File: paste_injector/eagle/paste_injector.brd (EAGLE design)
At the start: 40 x 30 mm, 20 parts, among them IC1 ULN2003AD, J2 USB, J5 PINHD-2X3, Q2 CSTCR6M00G53Z, U2 FT232RL, U4 ATMEGA328TQFP32

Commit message: Work in progress.
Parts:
- removed C5, C6, C7: 0.1uF, paste_injector:C0603
- removed U$28: OSH, paste_injector:OSH
- removed U2: FT232RL, paste_injector:SSOP28DB
- added C1: 0.1uF, paste_injector:C0603
- added JP2: (no value), paste_injector:1X06
- R10, R2: value 10K -> 5K
- moved R10 14.9 mm to (22.1, 5.74), turned to 270 degrees
- moved C3 14.3 mm to (6.01, 9.26), turned to 180 degrees
- moved U4 7.93 mm to (15.8, 14.1)
- moved C10 6.93 mm to (23.7, 12.6), turned to 90 degrees
- moved Q2 6.19 mm to (14.1, 22.0)
- moved C2 5.72 mm to (7.68, 16.3), turned to 270 degrees
- moved JP1 5.12 mm to (27.7, 27.9)
- moved IC1 4.92 mm to (28.9, 19.4), turned to 0 degrees
- moved LED1 1.38 mm to (16.4, 27.2)
- moved J5 0.90 mm to (4.45, 26.7)
- moved R1 0.64 mm to (31.8, 5.08)
- moved R2 0.45 mm to (12.4, 27.3)
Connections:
- removed net N$11: C6.1, U2.2
- removed net N$16: C7.1, U2.17
- removed net SER_RX: U2.1, U4.30
- removed net SER_TX: U2.5, U4.31
- removed net USB_DM: J2.2, U2.16
- removed net USB_DP: J2.3, U2.15
- new net DTR: C1.2, JP2.6
- new net RXI: JP2.4, U4.30
- new net TXO: JP2.5, U4.31
- net +5V: now also JP2.3; no longer C5.1, U2.20, U2.4
- net GND: now also JP2.1, JP2.2; no longer C5.2, C7.2, U2.18, U2.21, U2.25, U2.26, U2.7
- net RESET: now also C1.1; no longer C6.2

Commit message: Minor tweaks.
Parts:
- removed C10: 0.1uF, paste_injector:C0603
- removed IC1: ULN2003AD, paste_injector:SO16
- removed J5: PINHD-2X3, paste_injector:2X03
- removed JP1: (no value), paste_injector:1X05
- removed JP2: (no value), paste_injector:1X06
- removed LED1: (no value), arm-pro-mini-tester:LED0603
- removed Q2: CSTCR6M00G53Z, paste_injector:CSTCR6M
- removed R10: 5K, paste_injector:R0603
- removed U4: ATMEGA328TQFP32, paste_injector:TQFP32-08
- added C4: 0.1uF, paste_injector:C0603
- added D1: (no value), paste_injector:LED0603
- added ISP: PINHD-2X3, paste_injector:2X03
- added J1: USB, paste_injector:USB-MICRO-ZX62RD-AB-5P8
- added J3: (no value), paste_injector:1X05
- added Q1: CSTCR6M00G53Z, paste_injector:CSTCR6M
- added R3: 5K, paste_injector:R0603
- added U1: ATMEGA328TQFP32, paste_injector:TQFP32-08
- added U2: ULN2003AD, paste_injector:SO16
- C1: value 0.1uF -> 10uF; device paste_injector:C0603 -> paste_injector:A/3216-18R
- C3: value 10uF -> 0.1uF; device paste_injector:A/3216-18R -> paste_injector:C0603
- J2: value USB -> (none); device paste_injector:USB-MICRO-ZX62RD-AB-5P8 -> paste_injector:1X06
- R1: value (none) -> 10K; device paste_injector:CA9V -> paste_injector:TRIMPOT
- S1, S2: device paste_injector:TLE1105 -> paste_injector:PUSH_BUTTON
- moved J2 38.9 mm to (38.0, 21.1)
- moved C3 26.6 mm to (32.4, 12.6), turned to 0 degrees
- moved C1 24.6 mm to (7.94, 15.7), turned to 270 degrees
- moved C2 18.7 mm to (25.8, 11.6)
- moved S2 14.0 mm to (19.7, 4.19)
- moved S1 9.53 mm to (5.71, 4.19)
- moved R1 3.17 mm to (34.9, 5.08), turned to 0 degrees
- moved R2 1.77 mm to (11.7, 25.6)
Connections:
- net +5V: now also C1.+, C4.1, ISP.2, J1.1, J2.3, J3.3, R1.CW, R3.2, U1.18, U1.4, U1.6, U2.9; no longer C10.1, C3.+, IC1.9, J2.1, J5.2, JP1.3, JP2.3, R1.E, R10.2, U4.18, U4.4, U4.6
- net BACKWARD: now also S2.B1, U1.11; no longer S1.B, U4.11
- net DTR: now also C3.2, J2.6; no longer C1.2, JP2.6
- net FORWARD: now also S1.B1, U1.10; no longer S2.B, U4.10
- net GND: now also C1.-, C4.2, D1.C, ISP.6, J1.5, J2.1, J2.2, Q1.2, R1.CCW, S1.A1, S1.GND, S2.A1, S2.GND, U1.21, U1.3, U1.5, U2.5, U2.6, U2.7, U2.8; no longer C10.2, C3.-, IC1.5, IC1.6, IC1.7, IC1.8, J2.5, J5.6, JP2.1, JP2.2, LED1.C, Q2.2, R1.A, S1.A, S2.A, U4.21, U4.3, U4.5
- net M1: now also U1.32, U2.1; no longer IC1.1, U4.25
- net M1-BLUE: now also J3.5, U2.16; no longer IC1.16, JP1.5
- net M2: now also U1.1, U2.2; no longer IC1.2, U4.26
- net M2-PINK: now also J3.4, U2.15; no longer IC1.15, JP1.4
- net M3: now also U1.2, U2.3; no longer IC1.3, U4.19
- net M3-YELOW: now also J3.1, U2.14; no longer IC1.14, JP1.1
- net M4: now also U1.9, U2.4; no longer IC1.4, U4.22
- net M4-ORANGE: now also J3.2, U2.13; no longer IC1.13, JP1.2
- net MISO: now also ISP.1, U1.16; no longer J5.1, U4.16
- net MOSI: now also ISP.4, U1.15; no longer J5.4, U4.15
- net N$1: now also D1.A; no longer LED1.A
- net N$2: now also Q1.1, U1.7; no longer Q2.1, U4.7
- net N$7: now also Q1.3, U1.8; no longer Q2.3, U4.8
- net POT: now also R1.C, U1.23; no longer R1.S, U4.23
- net RESET: now also C3.1, ISP.5, R3.1, U1.29; no longer C1.1, J5.5, R10.1, U4.29
- net RXI: now also J2.4, U1.30; no longer JP2.4, U4.30
- net SCK/LED: now also ISP.3, U1.17; no longer J5.3, U4.17
- net TXO: now also J2.5, U1.31; no longer JP2.5, U4.31
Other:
- outline, holes or cut-outs redrawn
- board text added: "B"
- board text added: "O"
- board text added: "P"
- board text added: "PULL"
- board text added: "PUSH"
- board text added: "R"
- board text added: "REV 0"
- board text added: "SPD"
- board text added: "Y"

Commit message: Performed final routing.
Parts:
- moved S2 2.54 mm to (17.1, 4.19)
- moved C3 1.52 mm to (30.9, 12.6)
- moved R2 1.38 mm to (10.9, 24.5)
- moved Q1 1.36 mm to (15.7, 25.7)
- moved R3 1.19 mm to (22.2, 10.3)
- moved D1 0.84 mm to (7.92, 21.0), turned to 180 degrees
- moved C2 0.48 mm to (25.8, 11.1)
- turned ISP to 0 degrees
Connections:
- net GND: now also J1.A, J1.B, J1.C, J1.D
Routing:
- net +5V: track 0.00 -> 98.2 mm
- net M4: track 0.00 -> 56.8 mm, vias 0 -> 8
- net RESET: track 0.00 -> 46.3 mm, vias 0 -> 4
- net GND: track 0.00 -> 34.6 mm, vias 0 -> 3
- net RXI: track 0.00 -> 34.0 mm, vias 0 -> 2
- net MOSI: track 0.00 -> 28.2 mm, vias 0 -> 2
- net POT: track 0.00 -> 26.8 mm, vias 0 -> 2
- net MISO: track 0.00 -> 20.3 mm, vias 0 -> 4
- net SCK/LED: track 0.00 -> 19.9 mm
- net TXO: track 0.00 -> 19.2 mm, vias 0 -> 3
- net FORWARD: track 0.00 -> 18.7 mm, vias 0 -> 2
- net M2-PINK: track 0.00 -> 17.3 mm, vias 0 -> 2
- net M3: track 0.00 -> 16.4 mm, vias 0 -> 2
- net BACKWARD: track 0.00 -> 16.4 mm, vias 0 -> 2
- net M1-BLUE: track 0.00 -> 15.2 mm
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- added copper zone on layer 16, net GND
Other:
- board text added: "PUSH SPEED"
- board text removed: "SPD"

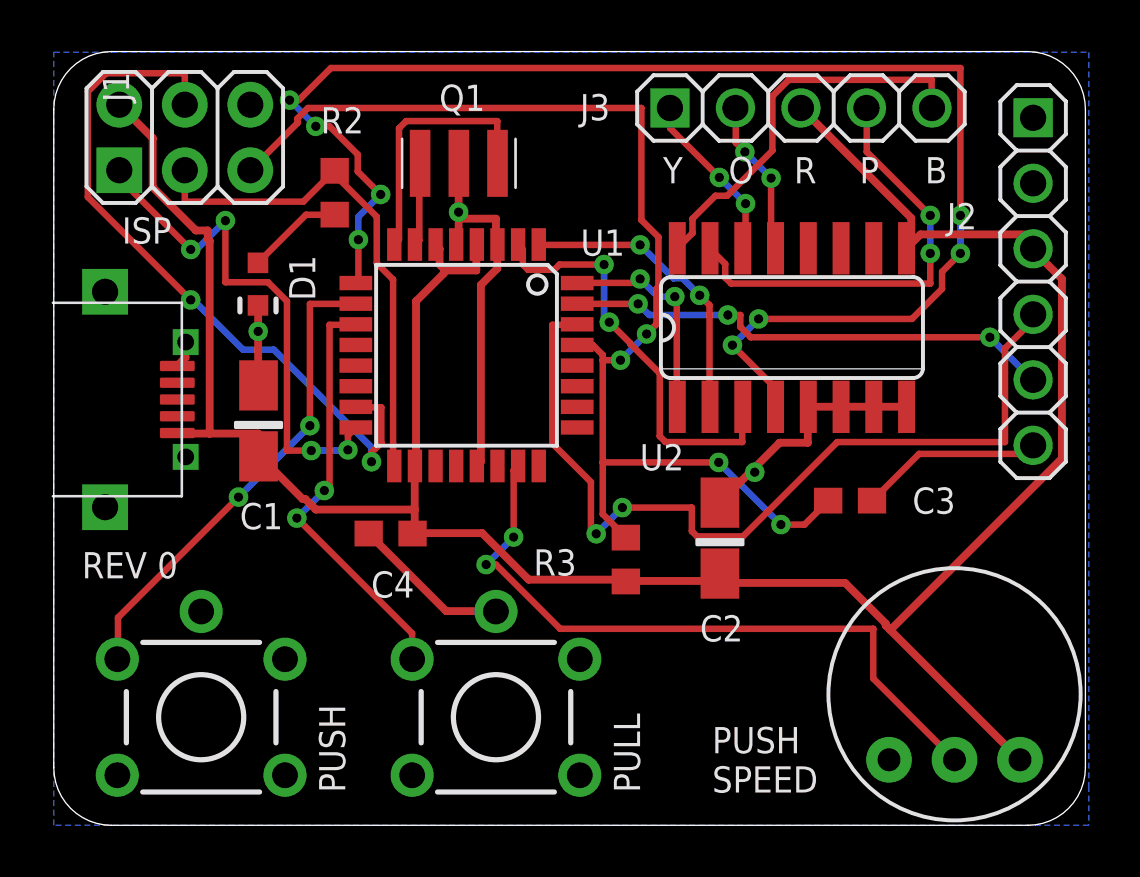
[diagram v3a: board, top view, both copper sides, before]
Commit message: Updated reasonator's footprint.
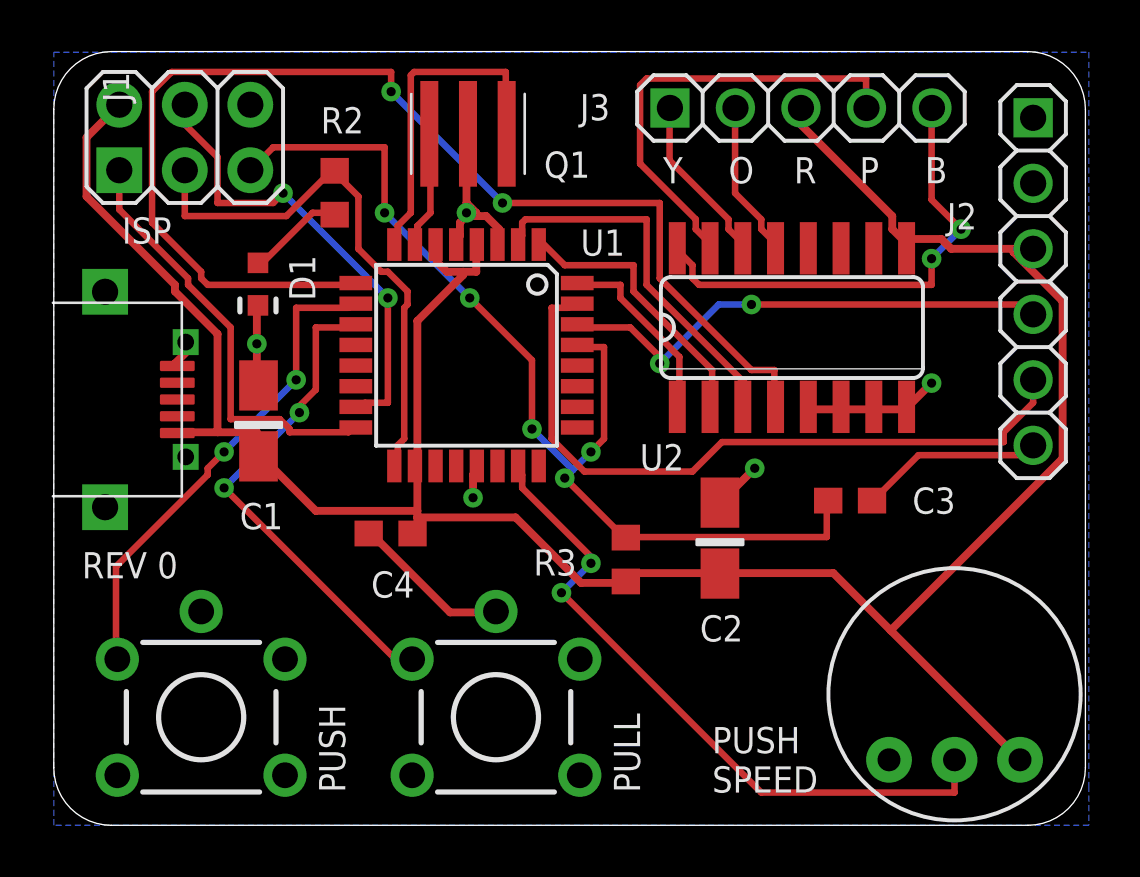
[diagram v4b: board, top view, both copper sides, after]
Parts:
- moved Q1 1.20 mm to (16.1, 26.8)
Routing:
- net RXI: track 34.0 -> 19.8 mm
- net MOSI: track 28.2 -> 18.2 mm
- net M4: track 56.8 -> 47.1 mm, vias 8 -> 2
- net TXO: track 19.2 -> 27.6 mm, vias 3 -> 0
- net GND: track 34.6 -> 26.4 mm, vias 3 -> 5
- net RESET: track 46.3 -> 40.6 mm, vias 4 -> 5
- net MISO: track 20.3 -> 16.7 mm, vias 4 -> 0
- net M1-BLUE: track 15.2 -> 18.7 mm, vias 0 -> 2
- net BACKWARD: track 16.4 -> 19.4 mm
- net N$7: track 10.1 -> 13.1 mm
- net +5V: track 98.2 -> 99.8 mm
- net M3: track 16.4 -> 14.8 mm, vias 2 -> 0
- net SCK/LED: track 19.9 -> 21.4 mm
- net N$2: track 3.23 -> 4.60 mm
- net M1: track 8.54 -> 7.50 mm, vias 2 -> 0
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
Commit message: Added BOM and TODO. Also, minor tweaks.
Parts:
- R2: value 5K -> 3K3
- R3: value 5K -> 10K
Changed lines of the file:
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@@
 <attribute name="NAME" x="2.6444" y="22.5552" size="1.016" layer="25" font="vector" ratio="10"/>
 </element>
-<element name="R3" library="paste_injector" package="R0603" value="5K" x="22.181" y="10.3042" smashed="yes" rot="R270">
+<element name="R3" library="paste_injector" package="R0603" value="10K" x="22.181" y="10.3042" smashed="yes" rot="R270">
 <attribute name="NAME" x="18.601" y="9.6842" size="1.016" layer="25" font="vector" ratio="10"/>
 </element>
@@
 <attribute name="VALUE" x="6.0124" y="21.6184" size="1.27" layer="27" rot="R270"/>
 </element>
-<element name="R2" library="paste_injector" package="R0603" value="5K" x="10.8918" y="24.5268" smashed="yes" rot="R90">
+<element name="R2" library="paste_injector" package="R0603" value="3K3" x="10.8918" y="24.5268" smashed="yes" rot="R90">
 <attribute name="NAME" x="10.3536" y="26.8272" size="1.016" layer="25" font="vector" ratio="10"/>
 </element>

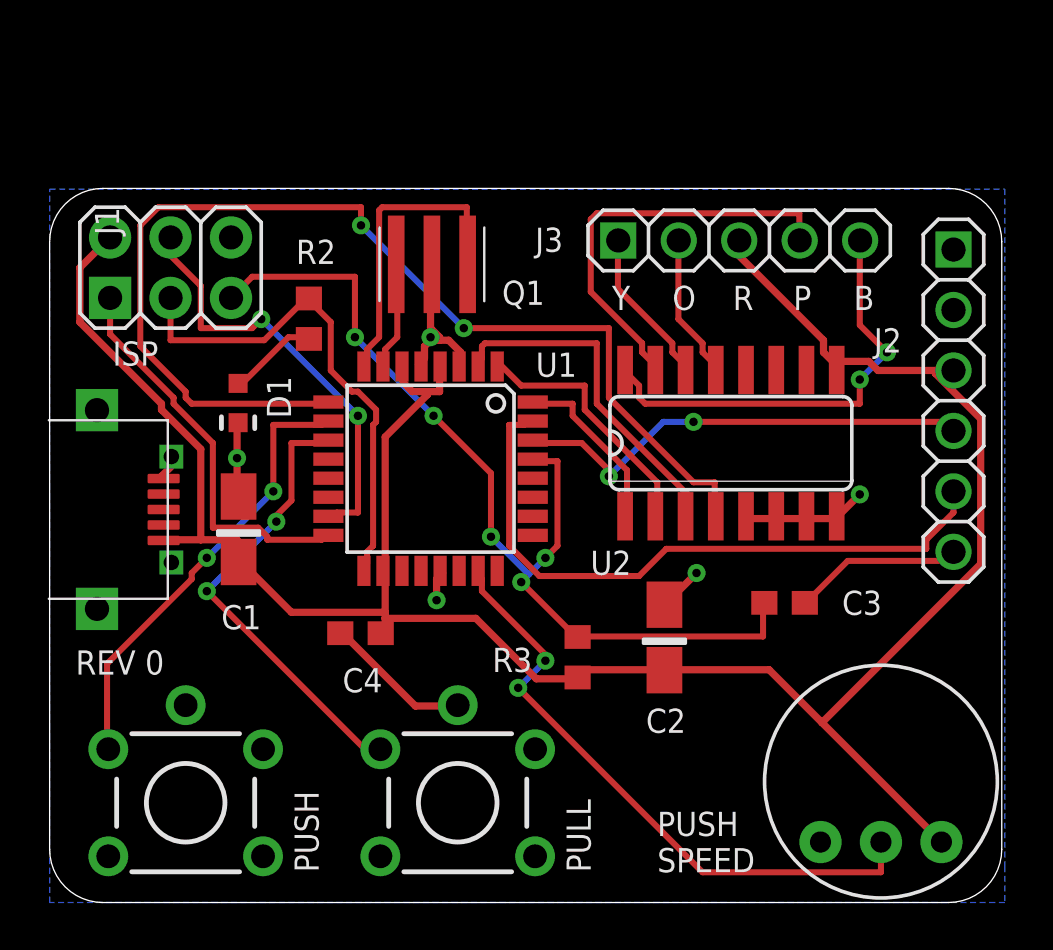
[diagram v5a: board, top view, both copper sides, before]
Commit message: Changed the board placement and rerouted (moved USB connector up) and push butto to the center.
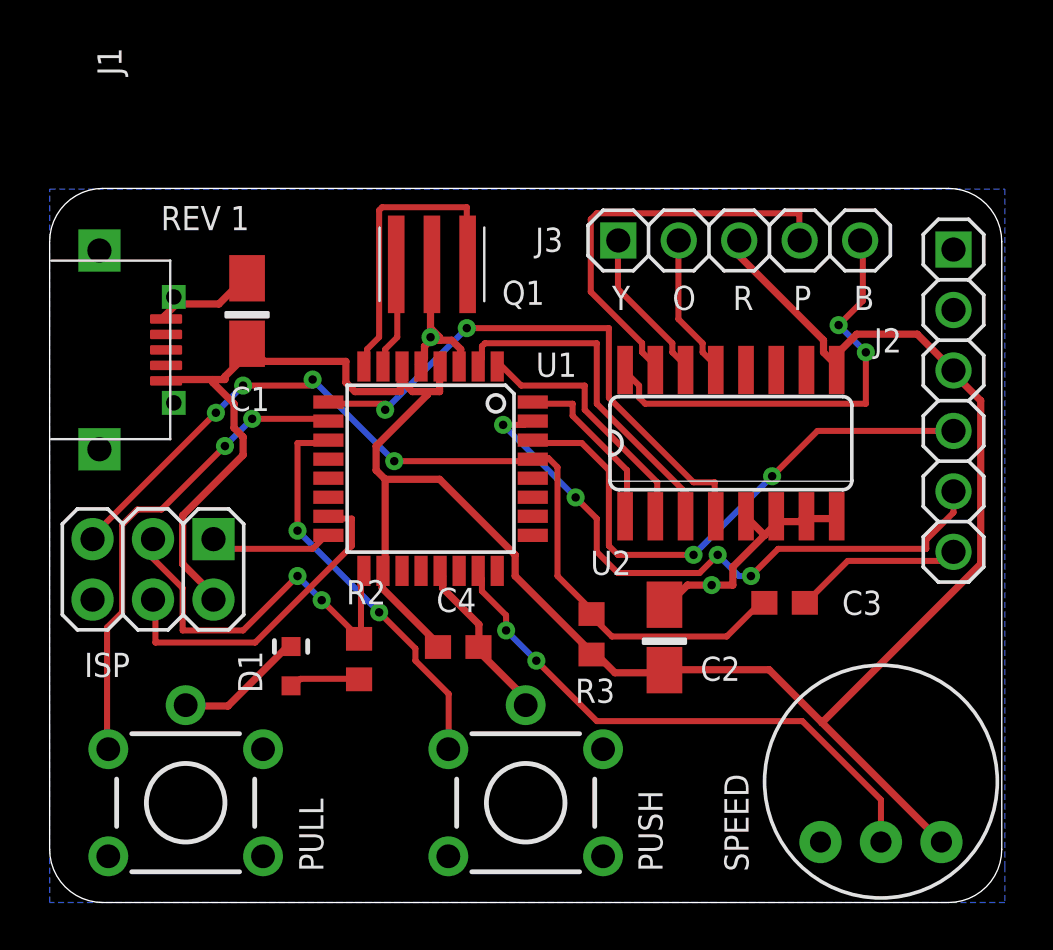
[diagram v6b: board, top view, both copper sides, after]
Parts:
- moved R2 14.5 mm to (13.0, 10.2)
- moved ISP 12.7 mm to (4.34, 14.0), turned to 180 degrees
- moved D1 11.3 mm to (10.1, 9.93), turned to 0 degrees
- moved C1 9.18 mm to (8.29, 24.9)
- moved J1 6.71 mm to (-0.53, 23.2)
- moved C4 4.15 mm to (17.2, 10.7), turned to 0 degrees
- moved S2 2.86 mm to (20.0, 4.19)
- moved R3 1.13 mm to (22.8, 11.3)
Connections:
- net BACKWARD renamed PUSH
- net FORWARD renamed PULL
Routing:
- net M4: track 47.1 -> 23.8 mm
- net MISO: track 16.7 -> 5.52 mm
- net GND: track 26.4 -> 35.8 mm, vias 5 -> 2
- net SCK/LED: track 21.4 -> 16.7 mm, vias 0 -> 2
- net MOSI: track 18.2 -> 14.0 mm, vias 2 -> 0
- net RXI: track 19.8 -> 23.7 mm
- net +5V: track 99.8 -> 103.0 mm
- net POT: track 26.4 -> 23.5 mm
- net PUSH: track 19.4 -> 16.8 mm
- net PULL: track 19.0 -> 20.3 mm
- net RESET: track 40.6 -> 39.5 mm, vias 5 -> 4
- net TXO: track 27.6 -> 26.6 mm, vias 0 -> 4
- net N$1: track 3.88 -> 3.09 mm
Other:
- board text added: "REV 1"
- board text added: "SPEED"
- board text removed: "PUSH SPEED"
- board text removed: "REV 0"

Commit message: Tweaked the design, updated the BOM.
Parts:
- removed C2: 10uF, paste_injector:A/3216-18R
- moved J1 41.1 mm to (40.6, 23.1), turned to 90 degrees
- moved J2 35.8 mm to (2.18, 20.4), turned to 90 degrees
- moved ISP 31.2 mm to (35.5, 13.9)
- moved C1 23.6 mm to (31.8, 22.1), turned to 90 degrees
- moved R2 8.69 mm to (21.5, 12.2)
- moved D1 8.54 mm to (18.4, 12.0)
- moved C4 6.59 mm to (10.6, 11.1)
- moved Q1 5.11 mm to (11.0, 26.8)
- moved U1 4.80 mm to (11.2, 18.3)
- moved U2 4.75 mm to (24.0, 20.6)
- moved R3 2.62 mm to (25.2, 12.1), turned to 90 degrees
- moved C3 2.52 mm to (28.4, 12.1), turned to 90 degrees
- moved J3 1.69 mm to (27.4, 28.4)
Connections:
- net +5V: no longer C2.+
- net GND: no longer C2.-
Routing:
- net MISO: track 5.52 -> 62.7 mm, vias 0 -> 6
- net DTR: track 7.37 -> 54.8 mm, vias 0 -> 4
- net MOSI: track 14.0 -> 57.0 mm, vias 0 -> 4
- net SCK/LED: track 16.7 -> 36.0 mm, vias 2 -> 4
- net TXO: track 26.6 -> 15.1 mm, vias 4 -> 2
- net RESET: track 39.5 -> 28.0 mm
- net +5V: track 103.0 -> 94.5 mm
- net RXI: track 23.7 -> 15.6 mm
- net GND: track 35.8 -> 30.2 mm, vias 2 -> 3
- net PUSH: track 16.8 -> 20.9 mm, vias 2 -> 0
- net POT: track 23.5 -> 27.6 mm
- net PULL: track 20.3 -> 17.3 mm, vias 2 -> 0
- net M2-PINK: track 17.5 -> 15.4 mm, vias 0 -> 2
- net M4: track 23.8 -> 21.9 mm, vias 2 -> 4
- net M3-YELOW: track 6.69 -> 4.90 mm
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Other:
- board text added: "FTDI"
